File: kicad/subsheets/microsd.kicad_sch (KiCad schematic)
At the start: 24 parts, among them Q1 FDN340P

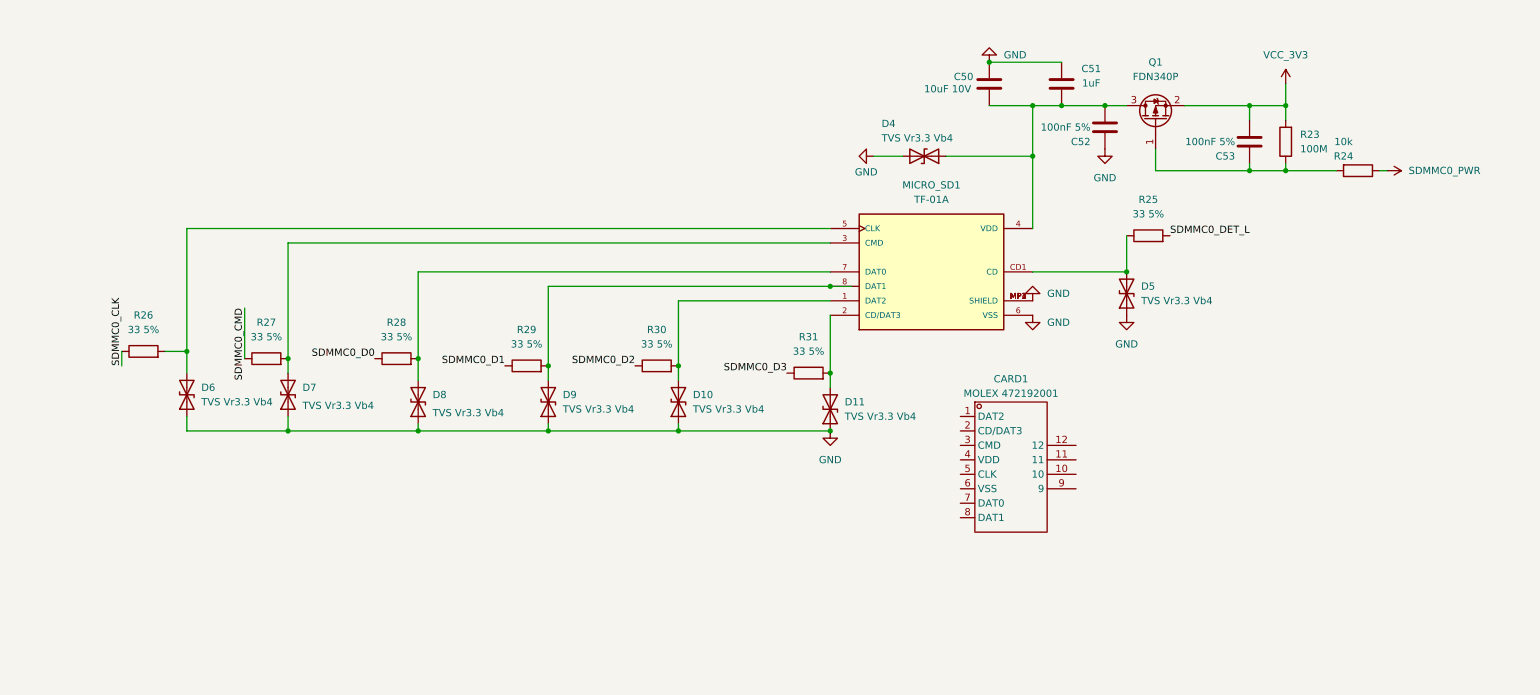
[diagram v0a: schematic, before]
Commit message: Resize sheets
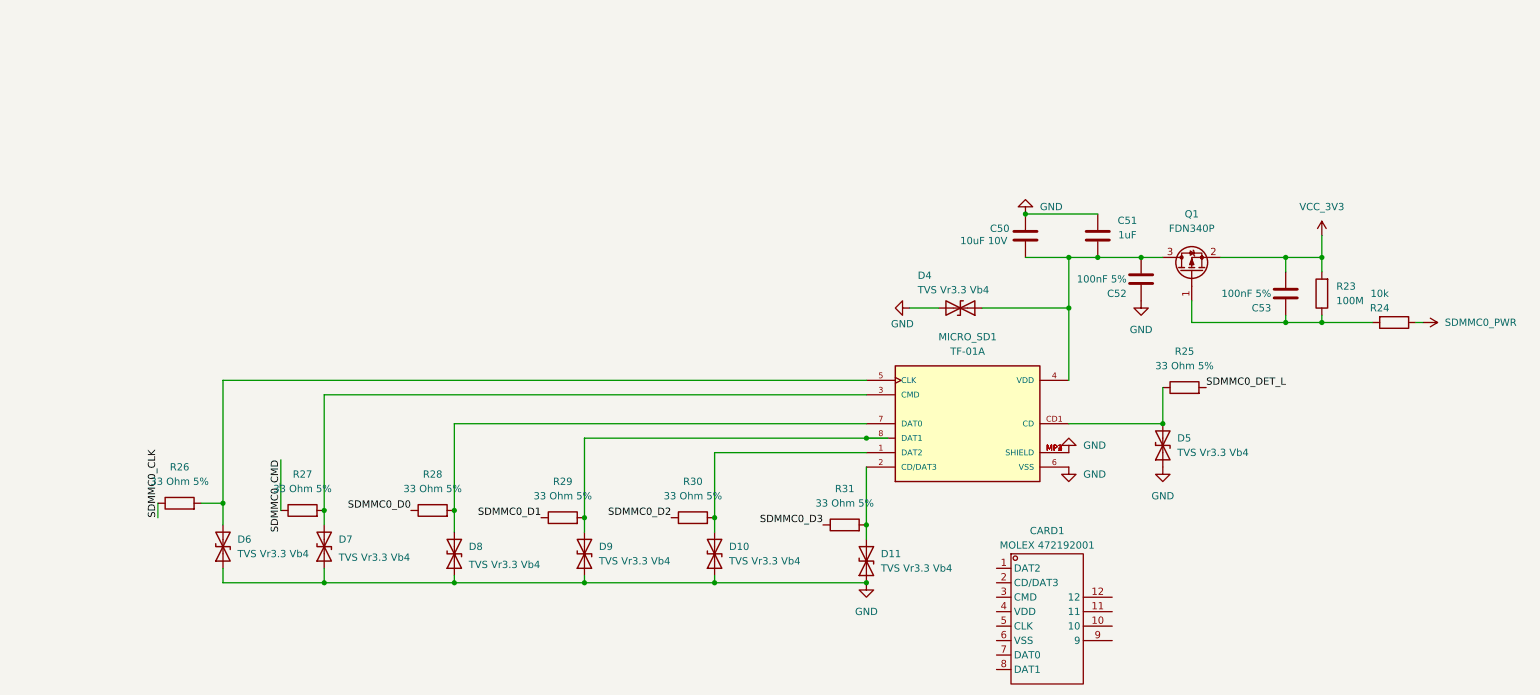
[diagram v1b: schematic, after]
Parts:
- R25, R26, R27, R28, R29, R30, R31: value 33 5% -> 33 Ohm 5%
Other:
- moved on the sheet: C50, C51, C52, C53, CARD1, D10, D11, D4, D5, D6, D7, D8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

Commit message: Wire microsd port
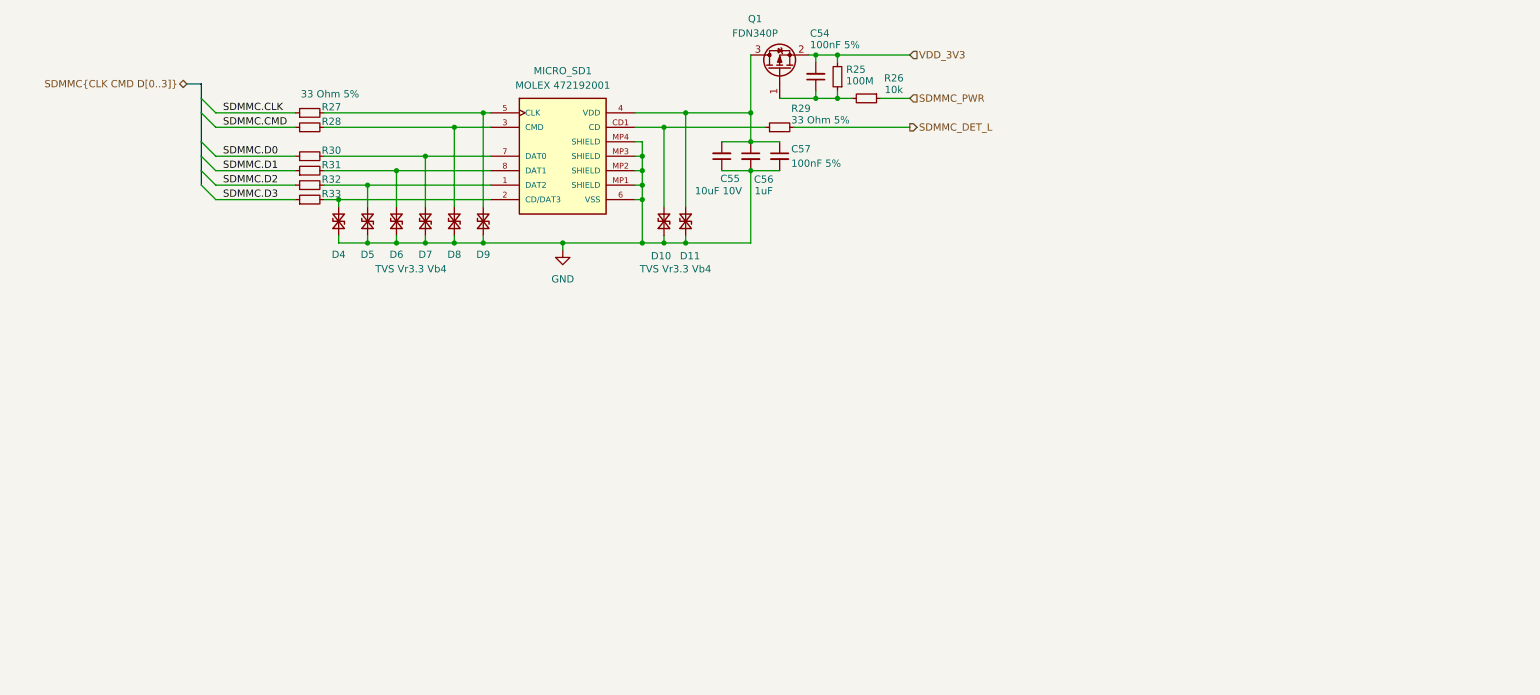
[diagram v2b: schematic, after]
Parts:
- removed CARD1: MOLEX 472192001, Connector_Card:microSD_HC_Molex_47219-2001, symbol MOLEX_4721920011-altium-import:root_0_472192001_
- removed D10, D11, D6, D7, D8, D9: TVS Vr3.3 Vb4, Resistor_SMD:R_0201_0603Metric, symbol Device:D_TVS
- removed R26, R27, R28, R29, R30, R31: 33 Ohm 5%, Resistor_SMD:R_0402_1005Metric, symbol Device:R
- added D4, D5, D6, D7, D8, D9: TVS Vr3.3 Vb4, Resistor_SMD:R_0201_0603Metric, symbol Device:D_TVS_Small
- added R27, R28, R30, R31, R32, R33: 33 Ohm 5%, Resistor_SMD:R_0402_1005Metric, symbol Device:R_Small
- C54: renamed from C53; symbol Device:C -> Device:C_Small
- C55: renamed from C50; symbol Device:C -> Device:C_Small
- C56: renamed from C51; symbol Device:C -> Device:C_Small
- C57: renamed from C52; symbol Device:C -> Device:C_Small
- D10: renamed from D5; symbol Device:D_TVS -> Device:D_TVS_Small
- D11: renamed from D4; symbol Device:D_TVS -> Device:D_TVS_Small
- MICRO_SD1: value TF-01A -> MOLEX 472192001; footprint TF-01A:TF-01A -> Connector_Card:microSD_HC_Molex_47219-2001
- R25: renamed from R23; symbol Device:R -> Device:R_Small
- R26: renamed from R24; symbol Device:R -> Device:R_Small
- R29: renamed from R25; symbol Device:R -> Device:R_Small
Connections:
- net GND: now also C57.2, D11.1 (A1), D4.1 (A1), D5.1 (A1), D6.1 (A1), D7.1 (A1), D8.1 (A1), D9.1 (A1); no longer C57.1, D11.2 (A2)
- net at MICRO_SD1.1 (DAT2): now also D5.2 (A2), R32.2
- net at MICRO_SD1.2 (CD/DAT3): now also D4.2 (A2), R33.2
- net at MICRO_SD1.7 (DAT0): now also D7.2 (A2), R30.2
- net at C55.2, C56.1, MICRO_SD1.4 (VDD)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: now also C57.1, D11.2 (A2); no longer C57.2, D11.1 (A1)
- net at MICRO_SD1.5 (CLK): now also D9.2 (A2), R27.2
- net at MICRO_SD1.3 (CMD): now also D8.2 (A2), R28.2
- net at MICRO_SD1.8 (DAT1): now also D6.2 (A2), R31.2
- net SDMMC0_DET_L renamed SDMMC_DET_L
- net SDMMC0_PWR renamed SDMMC_PWR
- net VCC_3V3 renamed VDD_3V3
- new net SDMMC.CLK: R27.1
- new net SDMMC.CMD: R28.1
- new net SDMMC.D0: R30.1
- new net SDMMC.D1: R31.1
- new net SDMMC.D2: R32.1
- new net SDMMC.D3: R33.1
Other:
- moved on the sheet: C54, C55, C56, C57, D10, D11, Q1, R25, R26, R29

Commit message: Clean up root sheet, add power supply subsheet
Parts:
- removed R29: 33 Ohm 5%, Resistor_SMD:R_0402_1005Metric, symbol Device:R_Small
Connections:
- no-connect marks 0 -> 1
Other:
- note added: "Would be SDMMC_DET_L Not needed as MicroSD always present"
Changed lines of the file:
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@@
 	(generator_version "9.0")
 	(paper "User" 200 120)
+	(text "Would be SDMMC_DET_L\nNot needed as MicroSD always present"
+		(exclude_from_sim no)
+		(at 144.018 38.1 0)
+		(effects
+			(font
+				(size 1 1)
+			)
+			(justify left)
+		)
+	)
 	(junction
 		(at 120.65 48.26)
@@
 		(diameter 0)
 		(color 0 0 0 0)
+	)
+	(no_connect
+		(at 142.24 38.1)
 	)
 	(bus_entry
@@
 		(pts
 			(xy 92.71 35.56) (xy 92.71 52.07)
-		)
-		(stroke
-			(width 0)
-			(type default)
-		)
-	)
-	(wire
-		(pts
-			(xy 147.32 38.1) (xy 167.64 38.1)
 		)
 		(stroke
@@
 			)
 			(justify left bottom)
-		)
-	)
-	(hierarchical_label "SDMMC_DET_L"
-		(shape output)
-		(at 167.64 38.1 0)
-		(effects
-			(font
-				(size 1.27 1.27)
-			)
-			(justify left)
 		)
 	)
@@
 					(unit 1)
 				)
-			)
-		)
-	)
-	(symbol
-		(lib_id "Device:R_Small")
-		(at 144.78 38.1 90)
-		(unit 1)
-		(exclude_from_sim no)
-		(in_bom yes)
-		(on_board yes)
-		(dnp no)
-		(property "Reference" "R29"
-			(at 146.812 34.798 90)
-			(effects
-				(font
-					(size 1.27 1.27)
-				)
-				(justify right)
-			)
-		)
-		(property "Value" "33 Ohm 5%"
-			(at 146.812 36.83 90)
-			(effects
-				(font
-					(size 1.27 1.27)
-				)
-				(justify right)
-			)
-		)
-		(property "Footprint" "Resistor_SMD:R_0402_1005Metric"
-			(at 144.78 38.1 0)
-			(effects
-				(font
-					(size 1.27 1.27)
-				)
-				(hide yes)
-			)
-		)
-		(property "Datasheet" "~"
-			(at 144.78 38.1 0)
-			(effects
-				(font
-					(size 1.27 1.27)
-				)
-				(hide yes)
-			)
-		)
-		(property "Description" "Resistor, small symbol"
-			(at 144.78 38.1 0)
-			(effects
-				(font
-					(size 1.27 1.27)
-				)
-				(hide yes)
-			)
-		)
-		(pin "1"
-		)
-		(pin "2"
-		)
-		(instances
-			(project "srad-camera"
-				(path "/da62c771-e8c9-451f-8df1-ec995aadcb11/f62984d3-000f-4116-a13f-09b83b0ce025"
-					(reference "R29")
-					(unit 1)
-				)

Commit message: Adjust root sheet
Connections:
- net SDMMC.CLK renamed CLK
- net SDMMC.CMD renamed CMD
- net SDMMC.D0 renamed D0
- net SDMMC.D1 renamed D1
- net SDMMC.D2 renamed D2
- net SDMMC.D3 renamed D3
- net SDMMC_PWR renamed PWR
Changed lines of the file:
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@@
 	)
 	(bus_entry
-		(at 43.18 45.72)
+		(at 50.8 45.72)
 		(size 2.54 2.54)
 		(stroke
@@
 	)
 	(bus_entry
-		(at 43.18 35.56)
+		(at 50.8 35.56)
 		(size 2.54 2.54)
 		(stroke
@@
 	)
 	(bus_entry
-		(at 43.18 40.64)
+		(at 50.8 40.64)
 		(size 2.54 2.54)
 		(stroke
@@
 	)
 	(bus_entry
-		(at 43.18 33.02)
+		(at 50.8 33.02)
 		(size 2.54 2.54)
 		(stroke
@@
 	)
 	(bus_entry
-		(at 43.18 48.26)
+		(at 50.8 48.26)
 		(size 2.54 2.54)
 		(stroke
@@
 	)
 	(bus_entry
-		(at 43.18 43.18)
+		(at 50.8 43.18)
 		(size 2.54 2.54)
 		(stroke
@@
 	(wire
 		(pts
-			(xy 45.72 43.18) (xy 59.69 43.18)
+			(xy 53.34 43.18) (xy 59.69 43.18)
 		)
 		(stroke
@@
 	(bus
 		(pts
-			(xy 43.18 30.48) (xy 43.18 33.02)
+			(xy 50.8 30.48) (xy 50.8 33.02)
 		)
 		(stroke
@@
 	(wire
 		(pts
-			(xy 45.72 38.1) (xy 59.69 38.1)
+			(xy 53.34 38.1) (xy 59.69 38.1)
 		)
 		(stroke
@@
 	(wire
 		(pts
-			(xy 45.72 45.72) (xy 59.69 45.72)
+			(xy 53.34 45.72) (xy 59.69 45.72)
 		)
 		(stroke
@@
 	(bus
 		(pts
-			(xy 43.18 43.18) (xy 43.18 45.72)
+			(xy 50.8 43.18) (xy 50.8 45.72)
 		)
 		(stroke
@@
 	(bus
 		(pts
-			(xy 43.18 45.72) (xy 43.18 48.26)
+			(xy 50.8 45.72) (xy 50.8 48.26)
 		)
 		(stroke
@@
 	(bus
 		(pts
-			(xy 43.18 35.56) (xy 43.18 40.64)
+			(xy 50.8 35.56) (xy 50.8 40.64)
 		)
 		(stroke
@@
 	(bus
 		(pts
-			(xy 43.18 40.64) (xy 43.18 43.18)
-		)
-		(stroke
-			(width 0)
-			(type default)
-		)
-	)
-	(wire
-		(pts
-			(xy 45.72 50.8) (xy 59.69 50.8)
+			(xy 50.8 40.64) (xy 50.8 43.18)
+		)
+		(stroke
+			(width 0)
+			(type default)
+		)
+	)
+	(wire
+		(pts
+			(xy 53.34 50.8) (xy 59.69 50.8)
 		)
 		(stroke
@@
 	(wire
 		(pts
-			(xy 45.72 48.26) (xy 59.69 48.26)
+			(xy 53.34 48.26) (xy 59.69 48.26)
 		)
 		(stroke
@@
 	(wire
 		(pts
-			(xy 45.72 35.56) (xy 59.69 35.56)
+			(xy 53.34 35.56) (xy 59.69 35.56)
 		)
 		(stroke
@@
 	(bus
 		(pts
-			(xy 43.18 33.02) (xy 43.18 35.56)
+			(xy 50.8 33.02) (xy 50.8 35.56)
 		)
 		(stroke
@@
 	(bus
 		(pts
-			(xy 40.64 30.48) (xy 43.18 30.48)
-		)
-		(stroke
-			(width 0)
-			(type default)
-		)
-	)
-	(label "SDMMC.CMD"
-		(at 46.99 38.1 0)
+			(xy 48.26 30.48) (xy 50.8 30.48)
+		)
+		(stroke
+			(width 0)
+			(type default)
+		)
+	)
+	(label "CMD"
+		(at 54.61 38.1 0)
 		(effects
 			(font
@@
 		)
 	)
-	(label "SDMMC.CLK"
-		(at 46.99 35.56 0)
+	(label "CLK"
+		(at 54.61 35.56 0)
 		(effects
 			(font
@@
 		)
 	)
-	(label "SDMMC.D0"
-		(at 46.99 43.18 0)
+	(label "D0"
+		(at 54.61 43.18 0)
 		(effects
 			(font
@@
 		)
 	)
-	(label "SDMMC.D3"
-		(at 46.99 50.8 0)
+	(label "D3"
+		(at 54.61 50.8 0)
 		(effects
 			(font
@@
 		)
 	)
-	(label "SDMMC.D2"
-		(at 46.99 48.26 0)
+	(label "D2"
+		(at 54.61 48.26 0)
 		(effects
 			(font
@@
 		)
 	)
-	(label "SDMMC.D1"
-		(at 46.99 45.72 0)
+	(label "D1"
+		(at 54.61 45.72 0)
 		(effects
 			(font
@@
 		)
 	)
-	(hierarchical_label "SDMMC{CLK CMD D[0..3]}"
+	(hierarchical_label "{SDMMC_BUS}"
 		(shape bidirectional)
-		(at 40.64 30.48 180)
+		(at 48.26 30.48 180)
 		(effects
 			(font
@@
 		)
 	)
-	(hierarchical_label "SDMMC_PWR"
+	(hierarchical_label "PWR"
 		(shape input)
 		(at 167.64 33.02 0)

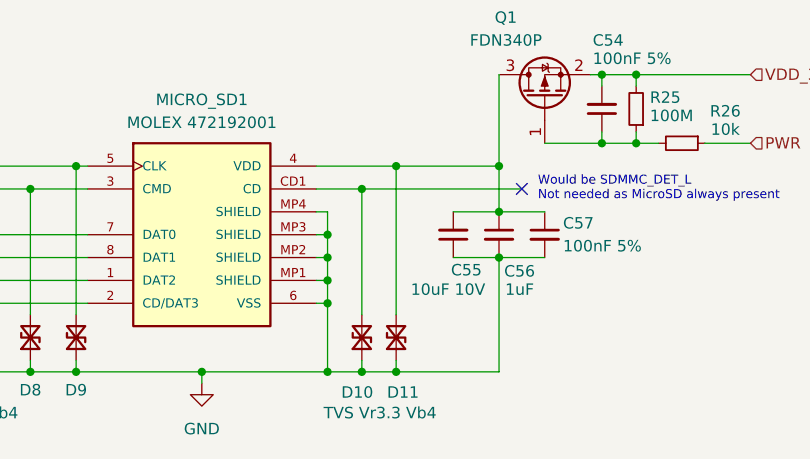
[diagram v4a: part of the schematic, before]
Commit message: Make sure logic levels are correct between ICs
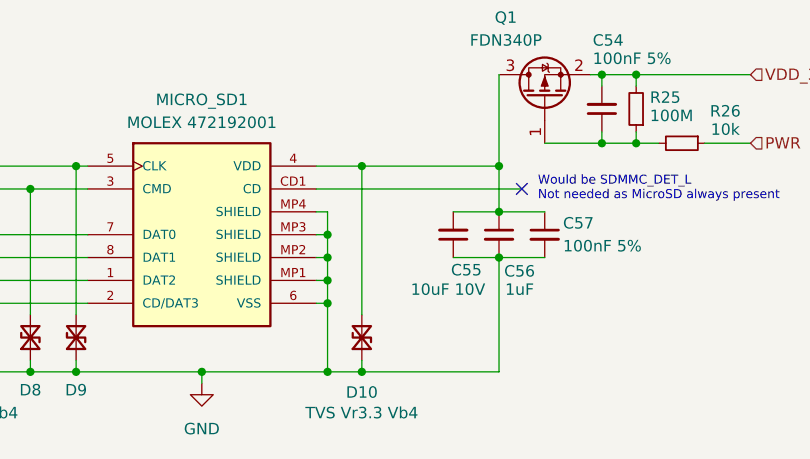
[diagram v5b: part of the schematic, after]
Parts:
- removed D11: TVS Vr3.3 Vb4, Resistor_SMD:R_0201_0603Metric, symbol Device:D_TVS_Small
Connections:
- net at D10.2 (A2): now also C55.2, C56.1, C57.1, MICRO_SD1.4 (VDD), Q1.3 (D); no longer MICRO_SD1.CD1 (CD)
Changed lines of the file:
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@@
-	)
-	(junction
-		(at 128.27 35.56)
-		(diameter 0)
-		(color 0 0 0 0)
 	)
 	(junction
@@
 	)
 	(junction
-		(at 124.46 38.1)
-		(diameter 0)
-		(color 0 0 0 0)
-	)
-	(junction
 		(at 120.65 43.18)
 		(diameter 0)
@@
 	)
 	(junction
-		(at 128.27 58.42)
-		(diameter 0)
-		(color 0 0 0 0)
-	)
-	(junction
 		(at 139.7 40.64)
+		(diameter 0)
+		(color 0 0 0 0)
+	)
+	(junction
+		(at 124.46 35.56)
 		(diameter 0)
 		(color 0 0 0 0)
@@
 	(wire
 		(pts
+			(xy 124.46 35.56) (xy 119.38 35.56)
+		)
+		(stroke
+			(width 0)
+			(type default)
+		)
+	)
+	(wire
+		(pts
 			(xy 139.7 35.56) (xy 139.7 25.4)
 		)
@@
 	(wire
 		(pts
-			(xy 124.46 38.1) (xy 124.46 52.07)
+			(xy 124.46 35.56) (xy 124.46 52.07)
 		)
 		(stroke
@@
 	(wire
 		(pts
-			(xy 128.27 35.56) (xy 119.38 35.56)
+			(xy 124.46 35.56) (xy 139.7 35.56)
 		)
 		(stroke
@@
 	(wire
 		(pts
-			(xy 128.27 35.56) (xy 139.7 35.56)
-		)
-		(stroke
-			(width 0)
-			(type default)
-		)
-	)
-	(wire
-		(pts
-			(xy 128.27 58.42) (xy 124.46 58.42)
+			(xy 124.46 58.42) (xy 139.7 58.42)
 		)
 		(stroke
@@
 	(wire
 		(pts
-			(xy 119.38 38.1) (xy 124.46 38.1)
+			(xy 119.38 38.1) (xy 142.24 38.1)
 		)
 		(stroke
@@
 	(wire
 		(pts
-			(xy 139.7 58.42) (xy 128.27 58.42)
-		)
-		(stroke
-			(width 0)
-			(type default)
-		)
-	)
-	(wire
-		(pts
 			(xy 119.38 48.26) (xy 120.65 48.26)
 		)
@@
 	(wire
 		(pts
-			(xy 124.46 38.1) (xy 142.24 38.1)
-		)
-		(stroke
-			(width 0)
-			(type default)
-		)
-	)
-	(wire
-		(pts
 			(xy 120.65 43.18) (xy 120.65 45.72)
 		)
@@
 	(wire
 		(pts
-			(xy 128.27 58.42) (xy 128.27 57.15)
-		)
-		(stroke
-			(width 0)
-			(type default)
-		)
-	)
-	(wire
-		(pts
 			(xy 151.13 25.4) (xy 149.86 25.4)
 		)
@@
 		(pts
 			(xy 92.71 58.42) (xy 106.68 58.42)
-		)
-		(stroke
-			(width 0)
-			(type default)
-		)
-	)
-	(wire
-		(pts
-			(xy 128.27 35.56) (xy 128.27 52.07)
 		)
 		(stroke
@@
 		(dnp no)
 		(property "Reference" "D10"
-			(at 125.73 60.706 90)
-			(effects
-				(font
-					(size 1.27 1.27)
-				)
-				(justify left)
+			(at 124.46 60.706 90)
+			(effects
+				(font
+					(size 1.27 1.27)
+				)
 			)
 		)
 		(property "Value" "TVS Vr3.3 Vb4"
-			(at 126.492 62.992 90)
+			(at 124.46 62.992 90)
 			(effects
 				(font
@@
 					(unit 1)
 				)
-			)
-		)
-	)
-	(symbol
-		(lib_id "Device:D_TVS_Small")
-		(at 128.27 54.61 90)
-		(unit 1)
-		(exclude_from_sim no)
-		(in_bom yes)
-		(on_board yes)
-		(dnp no)
-		(property "Reference" "D11"
-			(at 127.254 60.706 90)
-			(effects
-				(font
-					(size 1.27 1.27)
-				)
-				(justify right)
-			)
-		)
-		(property "Value" "TVS Vr3.3 Vb4"
-			(at 127.254 63.246 90)
-			(effects
-				(font
-					(size 1.27 1.27)
-				)
-				(justify right)
-				(hide yes)
-			)
-		)
-		(property "Footprint" "Resistor_SMD:R_0201_0603Metric"
-			(at 128.27 54.61 0)
-			(effects
-				(font
-					(size 1.27 1.27)
-				)
-				(hide yes)
-			)
-		)
-		(property "Datasheet" "~"
-			(at 128.27 54.61 0)
-			(effects
-				(font
-					(size 1.27 1.27)
-				)
-				(hide yes)
-			)
-		)
-		(property "Description" "Bidirectional transient-voltage-suppression diode, small symbol"
-			(at 128.27 54.61 0)
-			(effects
-				(font
-					(size 1.27 1.27)
-				)
-				(hide yes)
-			)
-		)
-		(pin "1"
-		)
-		(pin "2"
-		)
-		(instances
-			(project "srad-camera"
-				(path "/da62c771-e8c9-451f-8df1-ec995aadcb11/f62984d3-000f-4116-a13f-09b83b0ce025"
-					(reference "D11")
-					(unit 1)
-				)
